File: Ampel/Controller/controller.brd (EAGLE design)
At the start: 31.7 x 32.5 mm, 8 parts, among them IC1 ATtiny25

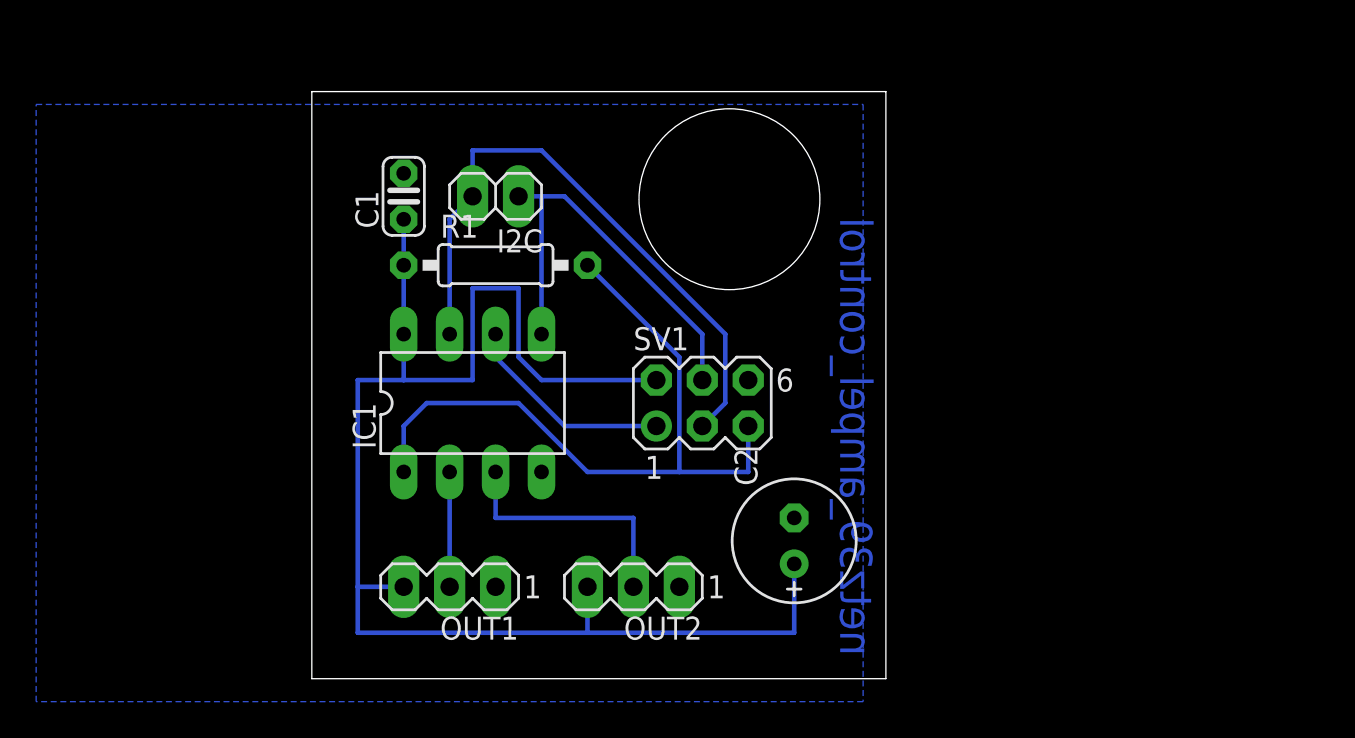
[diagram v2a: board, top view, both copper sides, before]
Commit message: Anpassung an Anschluss vom I2C-Adapter
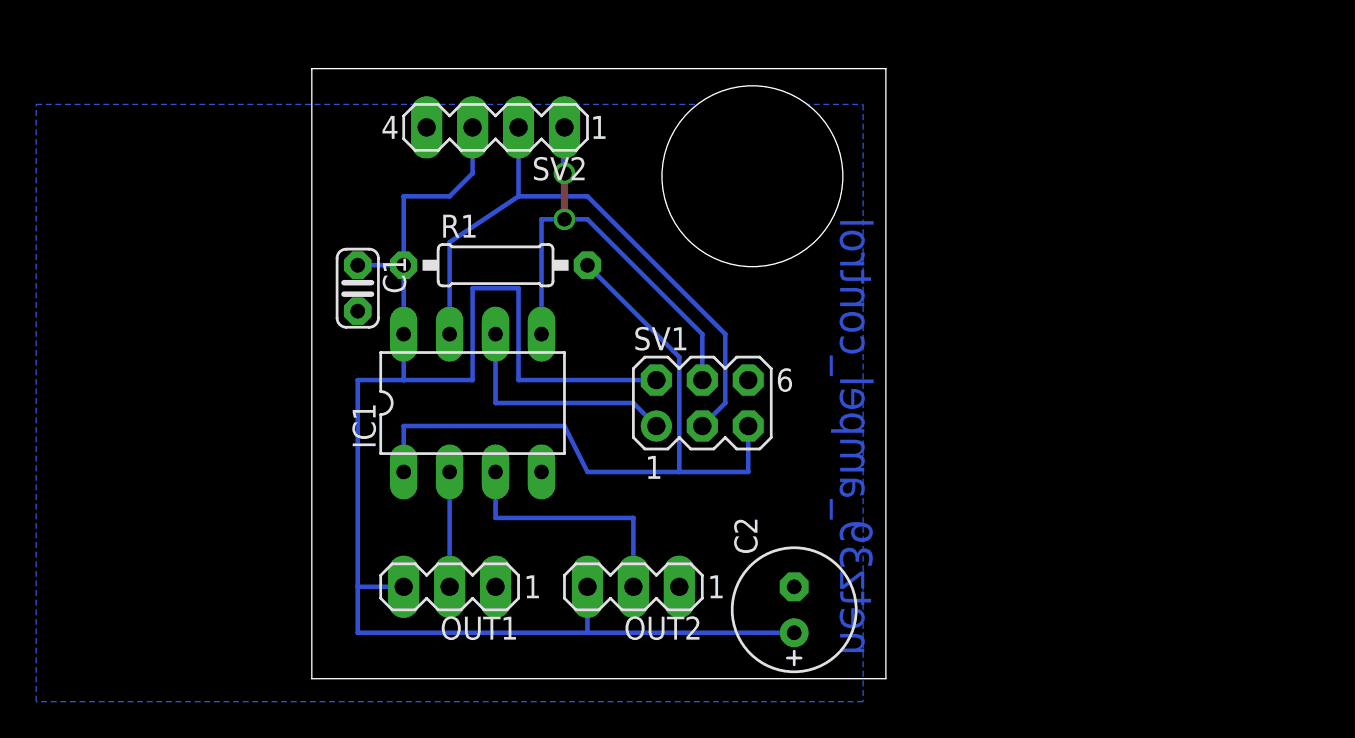
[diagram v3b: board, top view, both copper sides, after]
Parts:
- removed I2C: (no value), pinhead:1X02
- added SV2: (no value), con-lstb:MA04-1
- moved C1 5.68 mm to (2.54, 21.6), turned to 270 degrees
- moved C2 3.81 mm to (26.7, 3.81)
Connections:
- net GND: now also SV2.4
- net MOSI: now also SV2.1; no longer I2C.1
- net SCK: now also SV2.2; no longer I2C.2
- net VCC: now also SV2.3
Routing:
- net VCC: track 81.8 -> 89.4 mm
- net MOSI: track 23.5 -> 25.5 mm, vias 0 -> 2
- net MISO: track 11.7 -> 13.2 mm
- net SCK: track 34.5 -> 33.7 mm
- net RESET: track 39.8 -> 39.2 mm
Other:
- board size 31.7 x 32.5 mm -> 31.7 x 33.7 mm
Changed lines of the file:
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@@
 <plain>
 <wire x1="0" y1="0" x2="31.74" y2="0" width="0" layer="20"/>
-<wire x1="31.74" y1="0" x2="31.74" y2="32.46" width="0" layer="20"/>
-<wire x1="31.74" y1="32.46" x2="0" y2="32.46" width="0" layer="20"/>
-<wire x1="0" y1="32.46" x2="0" y2="0" width="0" layer="20"/>
-<hole x="23.09" y="26.51" drill="10"/>
+<wire x1="31.74" y1="0" x2="31.74" y2="33.73" width="0" layer="20"/>
+<wire x1="31.74" y1="33.73" x2="0" y2="33.73" width="0" layer="20"/>
+<wire x1="0" y1="33.73" x2="0" y2="0" width="0" layer="20"/>
+<hole x="24.36" y="27.78" drill="10"/>
 <text x="29.21" y="1.27" size="1.778" layer="16" font="vector" rot="MR90">netz39_ampel_control</text>
 </plain>
@@
 </element>
 <element name="R1" library="resistor" package="0207/10" value="10K" x="10.16" y="22.86"/>
-<element name="C1" library="resistor" package="C025-024X044" value="10n" x="5.08" y="26.67" rot="R90"/>
+<element name="C1" library="resistor" package="C025-024X044" value="10n" x="2.54" y="21.59" rot="R270"/>
 <element name="SV1" library="con-lstb" package="MA03-2" value="ISP" x="21.59" y="15.24">
 <attribute name="OC_NEWARK" value="unknown" x="40.64" y="-2.54" size="1.778" layer="27" display="off"/>
@@
 <attribute name="OC_FARNELL" value="unknown" x="17.78" y="5.08" size="1.778" layer="27" rot="R180" display="off"/>
 </element>
-<element name="I2C" library="pinhead" package="1X02" value="" x="10.16" y="26.67" rot="R180"/>
-<element name="C2" library="resistor" package="E2,5-7" value="100u" x="26.67" y="7.62" rot="R90"/>
+<element name="C2" library="resistor" package="E2,5-7" value="100u" x="26.67" y="3.81" rot="R90"/>
+<element name="SV2" library="con-lstb" package="MA04-1" value="" x="10.16" y="30.48" rot="R180">
+<attribute name="OC_NEWARK" value="unknown" x="10.16" y="30.48" size="1.778" layer="27" rot="R180" display="off"/>
+<attribute name="MPN" value="" x="10.16" y="30.48" size="1.778" layer="27" rot="R180" display="off"/>
+<attribute name="MF" value="" x="10.16" y="30.48" size="1.778" layer="27" rot="R180" display="off"/>
+<attribute name="OC_FARNELL" value="unknown" x="10.16" y="30.48" size="1.778" layer="27" rot="R180" display="off"/>
+</element>
 </elements>
 <signals>
@@
 <wire x1="2.54" y1="5.08" x2="2.54" y2="2.54" width="0.254" layer="16"/>
 <wire x1="5.08" y1="5.08" x2="2.54" y2="5.08" width="0.254" layer="16"/>
-<wire x1="12.7" y1="16.51" x2="19.05" y2="16.51" width="0.254" layer="16"/>
-<wire x1="11.43" y1="17.78" x2="12.7" y2="16.51" width="0.254" layer="16"/>
-<wire x1="11.43" y1="21.59" x2="11.43" y2="17.78" width="0.254" layer="16"/>
+<wire x1="26.67" y1="2.54" x2="15.24" y2="2.54" width="0.254" layer="16"/>
+<contactref element="SV2" pad="3"/>
+<wire x1="2.54" y1="22.86" x2="5.08" y2="22.86" width="0.254" layer="16"/>
+<wire x1="5.08" y1="22.86" x2="5.08" y2="26.67" width="0.254" layer="16"/>
+<wire x1="5.08" y1="26.67" x2="7.62" y2="26.67" width="0.254" layer="16"/>
+<wire x1="7.62" y1="26.67" x2="8.89" y2="27.94" width="0.254" layer="16"/>
+<wire x1="8.89" y1="27.94" x2="8.89" y2="30.48" width="0.254" layer="16"/>
+<wire x1="5.08" y1="16.51" x2="8.89" y2="16.51" width="0.254" layer="16"/>
+<wire x1="8.89" y1="16.51" x2="8.89" y2="21.59" width="0.254" layer="16"/>
 <wire x1="8.89" y1="21.59" x2="11.43" y2="21.59" width="0.254" layer="16"/>
-<wire x1="8.89" y1="16.51" x2="8.89" y2="21.59" width="0.254" layer="16"/>
-<wire x1="5.08" y1="16.51" x2="8.89" y2="16.51" width="0.254" layer="16"/>
-<wire x1="26.67" y1="6.35" x2="26.67" y2="2.54" width="0.254" layer="16"/>
-<wire x1="26.67" y1="2.54" x2="15.24" y2="2.54" width="0.254" layer="16"/>
-<wire x1="5.08" y1="22.86" x2="5.08" y2="25.4" width="0.254" layer="16"/>
+<wire x1="11.43" y1="21.59" x2="11.43" y2="16.51" width="0.254" layer="16"/>
+<wire x1="11.43" y1="16.51" x2="19.05" y2="16.51" width="0.254" layer="16"/>
 </signal>
 <signal name="GND">
@@
 </polygon>
 <contactref element="C2" pad="-"/>
+<contactref element="SV2" pad="4"/>
+<wire x1="10.16" y1="5.08" x2="12.7" y2="11.43" width="0" layer="19" extent="1-1"/>
 </signal>
 <signal name="RESET">
@@
 <contactref element="IC1" pad="1"/>
 <contactref element="SV1" pad="5"/>
-<wire x1="6.35" y1="15.24" x2="5.08" y2="13.97" width="0.254" layer="16"/>
 <wire x1="5.08" y1="13.97" x2="5.08" y2="11.43" width="0.254" layer="16"/>
-<wire x1="11.43" y1="15.24" x2="6.35" y2="15.24" width="0.254" layer="16"/>
-<wire x1="15.24" y1="11.43" x2="11.43" y2="15.24" width="0.254" layer="16"/>
 <wire x1="24.13" y1="11.43" x2="20.32" y2="11.43" width="0.254" layer="16"/>
 <wire x1="20.32" y1="11.43" x2="15.24" y2="11.43" width="0.254" layer="16"/>
@@
 <wire x1="20.32" y1="17.78" x2="15.24" y2="22.86" width="0.254" layer="16"/>
 <wire x1="20.32" y1="11.43" x2="20.32" y2="17.78" width="0.254" layer="16"/>
+<wire x1="5.08" y1="13.97" x2="13.97" y2="13.97" width="0.254" layer="16"/>
+<wire x1="13.97" y1="13.97" x2="15.24" y2="11.43" width="0.254" layer="16"/>
 </signal>
 <signal name="MISO">
 <contactref element="SV1" pad="1"/>
 <contactref element="IC1" pad="6"/>
-<wire x1="10.16" y1="17.78" x2="10.16" y2="19.05" width="0.254" layer="16"/>
-<wire x1="13.97" y1="13.97" x2="10.16" y2="17.78" width="0.254" layer="16"/>
-<wire x1="19.05" y1="13.97" x2="13.97" y2="13.97" width="0.254" layer="16"/>
+<wire x1="10.16" y1="19.05" x2="10.16" y2="15.24" width="0.254" layer="16"/>
+<wire x1="10.16" y1="15.24" x2="17.78" y2="15.24" width="0.254" layer="16"/>
+<wire x1="17.78" y1="15.24" x2="19.05" y2="13.97" width="0.254" layer="16"/>
 </signal>
 <signal name="SCK">
 <contactref element="SV1" pad="3"/>
 <contactref element="IC1" pad="7"/>
-<contactref element="I2C" pad="2"/>
-<wire x1="8.89" y1="26.67" x2="7.62" y2="25.4" width="0.254" layer="16"/>
-<wire x1="7.62" y1="25.4" x2="7.62" y2="19.05" width="0.254" layer="16"/>
+<wire x1="7.62" y1="24.13" x2="7.62" y2="19.05" width="0.254" layer="16"/>
 <wire x1="22.86" y1="15.24" x2="21.59" y2="13.97" width="0.254" layer="16"/>
 <wire x1="22.86" y1="19.05" x2="22.86" y2="15.24" width="0.254" layer="16"/>
-<wire x1="12.7" y1="29.21" x2="22.86" y2="19.05" width="0.254" layer="16"/>
-<wire x1="8.89" y1="29.21" x2="12.7" y2="29.21" width="0.254" layer="16"/>
-<wire x1="8.89" y1="26.67" x2="8.89" y2="29.21" width="0.254" layer="16"/>
+<wire x1="15.24" y1="26.67" x2="22.86" y2="19.05" width="0.254" layer="16"/>
+<contactref element="SV2" pad="2"/>
+<wire x1="7.62" y1="24.13" x2="11.43" y2="26.67" width="0.254" layer="16"/>
+<wire x1="11.43" y1="26.67" x2="15.24" y2="26.67" width="0.254" layer="16"/>
+<wire x1="11.43" y1="30.48" x2="11.43" y2="26.67" width="0.254" layer="16"/>
 </signal>
 <signal name="MOSI">
 <contactref element="SV1" pad="4"/>
 <contactref element="IC1" pad="5"/>
-<contactref element="I2C" pad="1"/>
-<wire x1="12.7" y1="26.67" x2="12.7" y2="19.05" width="0.254" layer="16"/>
+<wire x1="12.7" y1="25.4" x2="12.7" y2="19.05" width="0.254" layer="16"/>
 <wire x1="21.59" y1="19.05" x2="21.59" y2="16.51" width="0.254" layer="16"/>
-<wire x1="13.97" y1="26.67" x2="21.59" y2="19.05" width="0.254" layer="16"/>
-<wire x1="11.43" y1="26.67" x2="12.7" y2="26.67" width="0.254" layer="16"/>
-<wire x1="12.7" y1="26.67" x2="13.97" y2="26.67" width="0.254" layer="16"/>
+<wire x1="15.24" y1="25.4" x2="21.59" y2="19.05" width="0.254" layer="16"/>
+<wire x1="12.7" y1="25.4" x2="13.97" y2="25.4" width="0.254" layer="16"/>
+<contactref element="SV2" pad="1"/>
+<wire x1="13.97" y1="25.4" x2="15.24" y2="25.4" width="0.254" layer="16"/>
+<wire x1="13.97" y1="30.48" x2="13.97" y2="29.21" width="0.254" layer="16"/>
+<wire x1="13.97" y1="29.21" x2="13.97" y2="27.94" width="0.4064" layer="16"/>
+<via x="13.97" y="27.94" extent="1-16" drill="0.8" diameter="0.254" shape="square"/>
+<via x="13.97" y="25.4" extent="1-16" drill="0.8" diameter="0.254" shape="square"/>
+<wire x1="13.97" y1="27.94" x2="13.97" y2="25.4" width="0.4064" layer="1"/>
 </signal>
 <signal name="N$1">

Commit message: letzte Anpassungen zum Ätzen
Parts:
- moved C1 15.2 mm to (17.8, 21.6)
- moved OUT2 15.2 mm to (33.0, 5.08)
- moved IC1 15.2 mm to (24.1, 15.2)
- moved OUT1 15.2 mm to (22.9, 5.08)
- moved R1 15.2 mm to (25.4, 22.9)
- moved SV1 15.2 mm to (36.8, 15.2)
- moved SV2 15.2 mm to (25.4, 30.5)
- moved C2 15.2 mm to (41.9, 3.81)

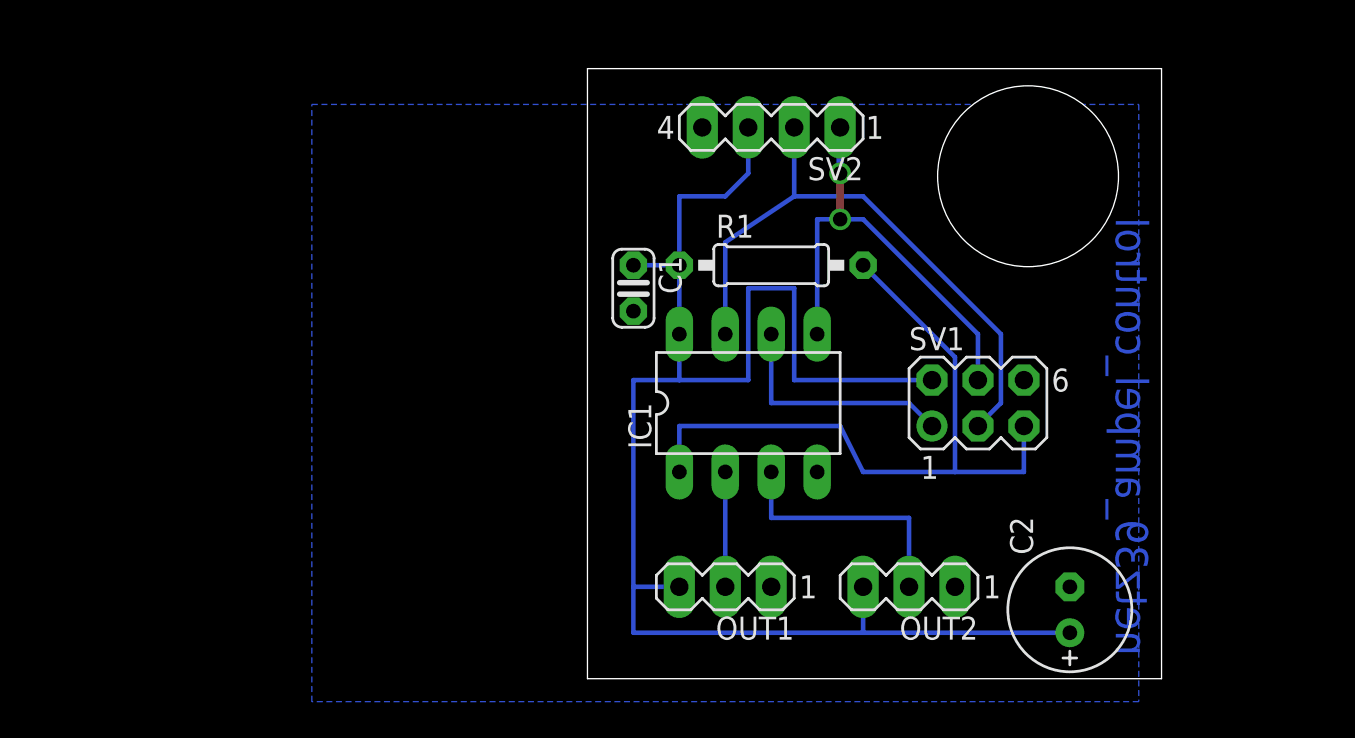
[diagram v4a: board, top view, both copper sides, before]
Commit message: Adapter: stecker angepasst Controller: board redesign
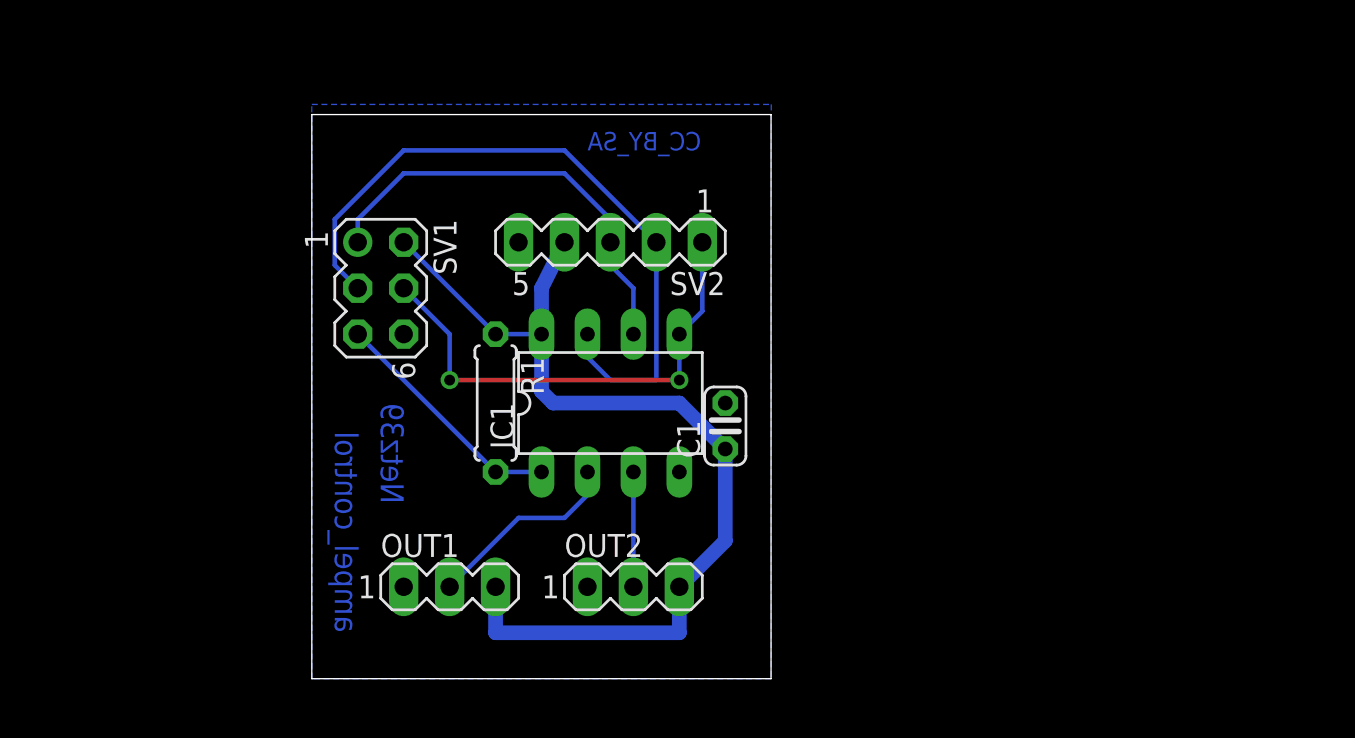
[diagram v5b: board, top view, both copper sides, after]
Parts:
- removed C2: 100u, resistor:E2,5-7
- R1: device resistor:0207/10 -> resistor:0207/7
- SV2: device con-lstb:MA04-1 -> con-lstb:MA05-1
- moved SV1 33.6 mm to (3.81, 21.6), turned to 270 degrees
- moved R1 17.0 mm to (10.2, 15.2), turned to 270 degrees
- moved OUT2 15.2 mm to (17.8, 5.08), turned to 0 degrees
- moved OUT1 15.2 mm to (7.62, 5.08), turned to 0 degrees
- moved SV2 10.9 mm to (16.5, 24.1)
- moved C1 9.16 mm to (22.9, 14.0), turned to 90 degrees
- moved IC1 7.62 mm to (16.5, 15.2)
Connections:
- net GND: now also SV2.5; no longer C2.-, SV2.4
- net MISO: now also SV2.3
- net VCC: now also SV2.4; no longer C2.+, SV2.3
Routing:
- net VCC: track 89.4 -> 53.7 mm
- net RESET: track 39.2 -> 13.3 mm
- net MISO: track 13.2 -> 24.2 mm
- net N$1: track 14.0 -> 6.35 mm
- net SCK: track 33.7 -> 39.0 mm
- net N$2: track 6.35 -> 11.0 mm
- net MOSI: track 25.5 -> 27.0 mm, vias 2 -> 0
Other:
- board size 31.7 x 33.7 mm -> 25.4 x 31.2 mm
- board text added: "CC_BY_SA"
- board text added: "Netz39"
- board text added: "ampel_control"
- board text removed: "netz39_ampel_control"
